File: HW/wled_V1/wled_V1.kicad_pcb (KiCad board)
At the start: 2 copper layers, 44.6 x 77.3 mm, 25 parts, among them J1 0031.8201, U3 TXS0102DCT

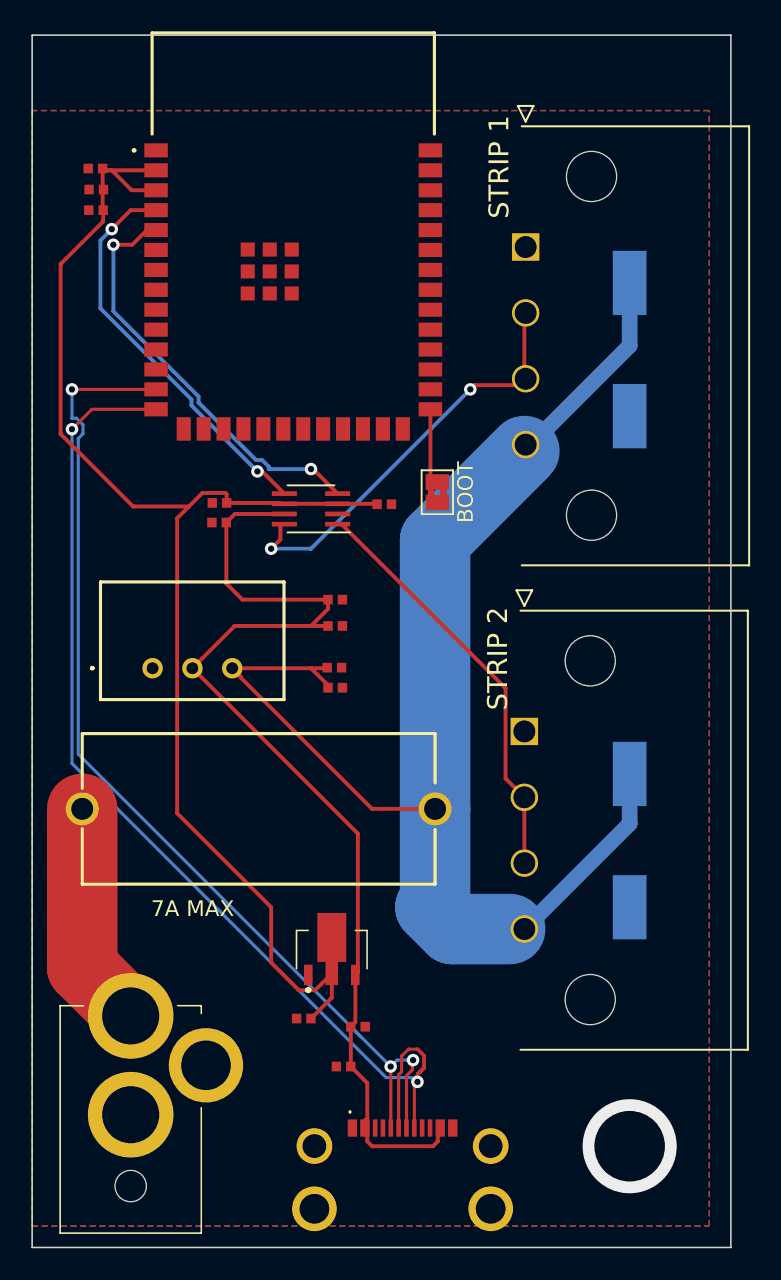
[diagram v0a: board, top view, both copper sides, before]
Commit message: new parts and routing
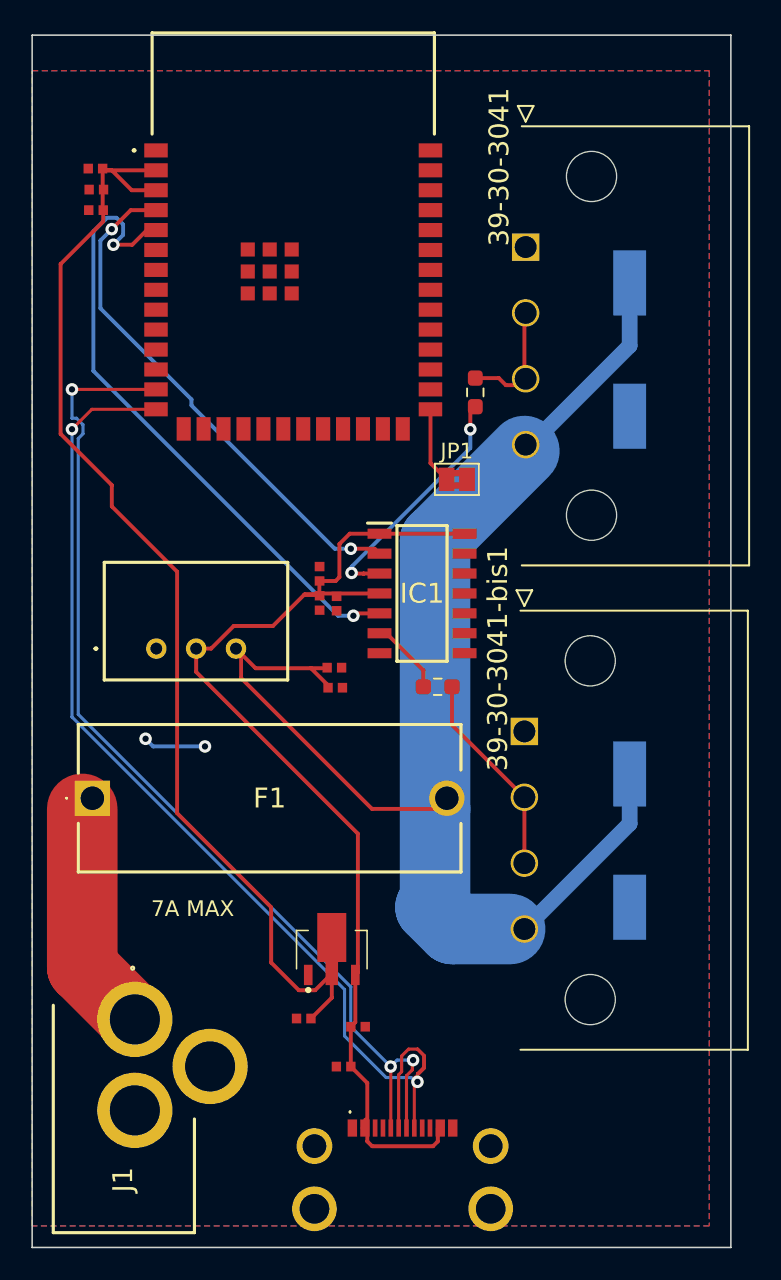
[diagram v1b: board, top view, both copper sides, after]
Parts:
- removed C2, C6: 100nF, SamacSys_Parts:CAPC1005X55N
- removed PJ-057AH1: Jack-DC, SamacSys_Parts:PJ057AH
- removed U3: TXS0102DCT, Package_SO:SSOP-8_2.95x2.8mm_P0.65mm
- added F1: BK1_HTC-100M, SamacSys_Parts:BK1HTC100M, F.Cu at (108.0, 117.5)
- added IC1: SN74AHCT125DR, SamacSys_Parts:SOIC127P600X175-14N, F.Cu at (129.0, 104.5)
- added R1: 0, Resistor_SMD:R_0603_1608Metric_Pad0.98x0.95mm_HandSolder, F.Cu at (132.4, 91.6)
- added R2: 0, Resistor_SMD:R_0603_1608Metric_Pad0.98x0.95mm_HandSolder, F.Cu at (130.0, 110.4)
- 39-30-3041: renamed from STRIP 1
- 39-30-3041-bis1: renamed from STRIP 2
- C5, C8: footprint SamacSys_Parts:CAPAE1030X1030N -> SamacSys_Parts:CAPAE1030X1050N
- J1: value 0031.8201 -> 694106301002; footprint SamacSys_Parts:0031.8201 -> SamacSys_Parts:694106301002_1
- moved J1 27.3 mm to (114.5, 145.2), turned to 90 degrees
- moved C4 9.10 mm to (123.6, 105.1), turned to -90 degrees
- moved C1 1.93 mm to (122.5, 103.2), turned to 90 degrees
- moved C12 1.77 mm to (122.5, 105.1), turned to -90 degrees
- moved JP1 1.49 mm to (131.2, 97.2), turned to 0 degrees
- moved TSR-1-2450 1.27 mm to (112.1, 108.0)
- renumbered BOOT to JP1
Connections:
- J1 pad 2: +12V -> GND
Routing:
- net Net-(39-30-3041-Pin_2): track 26.5 -> 7.52 mm, vias 2 -> 0
- net +3.3V: track 88.9 -> 72.8 mm
- net D3_5V: track 0.00 -> 15.3 mm, vias 0 -> 2
- net D4: track 26.8 -> 40.2 mm
- net Net-(39-30-3041-bis1-Pin_2): track 26.4 -> 13.2 mm
- net D3: track 25.5 -> 33.2 mm
- net D4_5V: track 0.00 -> 4.39 mm
- net GND: track 0.44 -> 3.99 mm, vias 0 -> 2
- net Net-(J1-POWER): track 16.1 -> 14.5 mm
- net +5V: track 68.0 -> 69.0 mm
- net D-: track 68.4 -> 67.4 mm
- net (no net): vias 1 -> 0

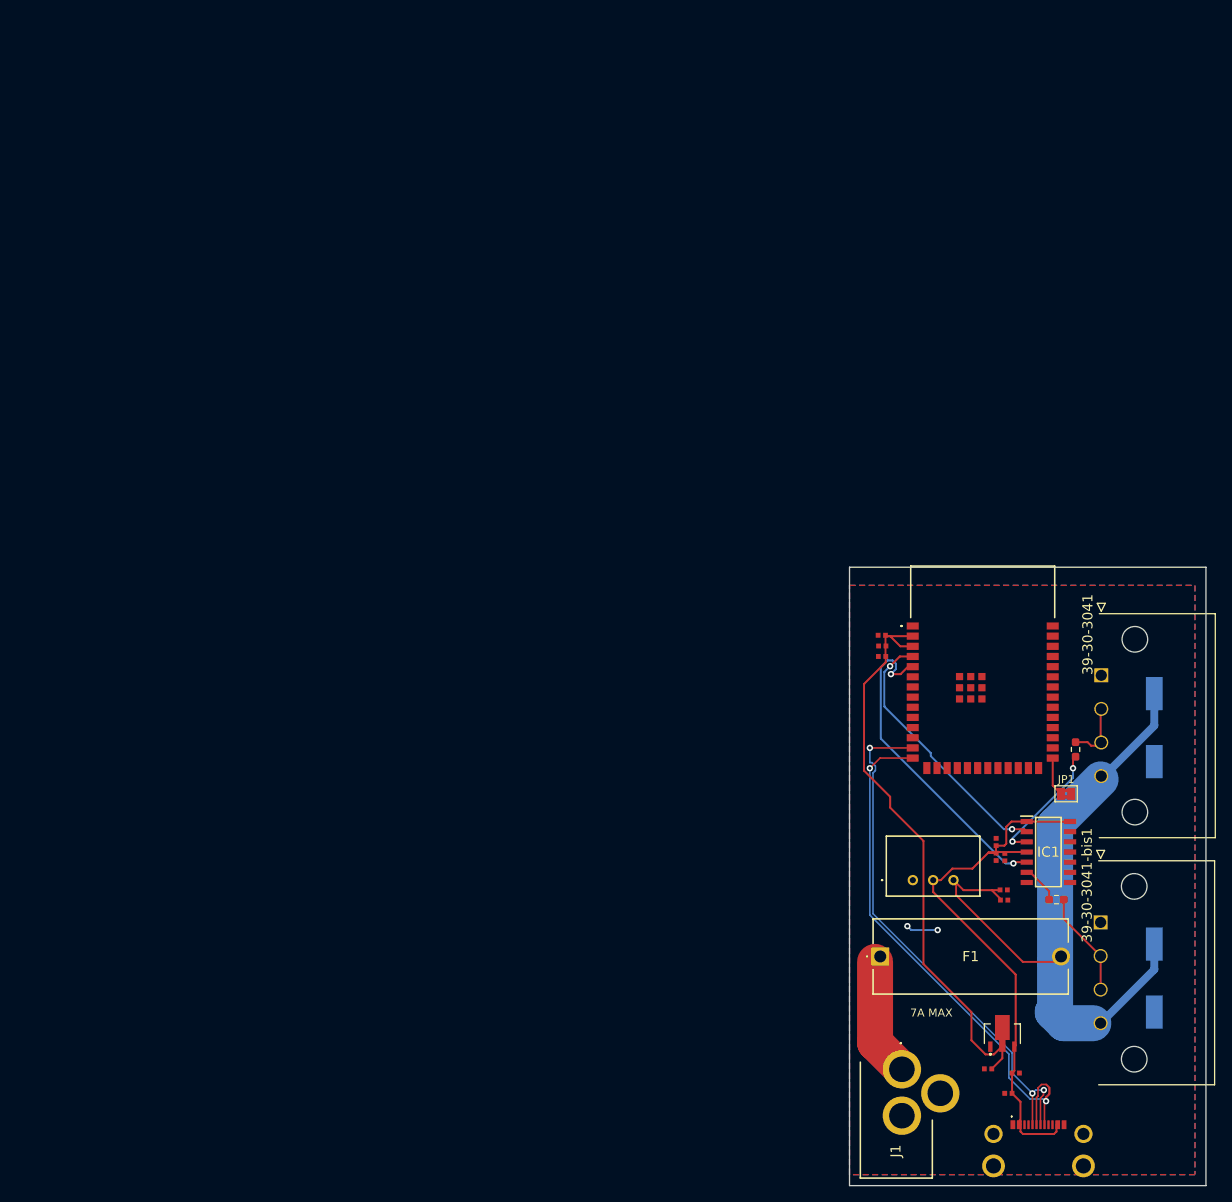
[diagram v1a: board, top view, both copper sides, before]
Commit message: mounting points added
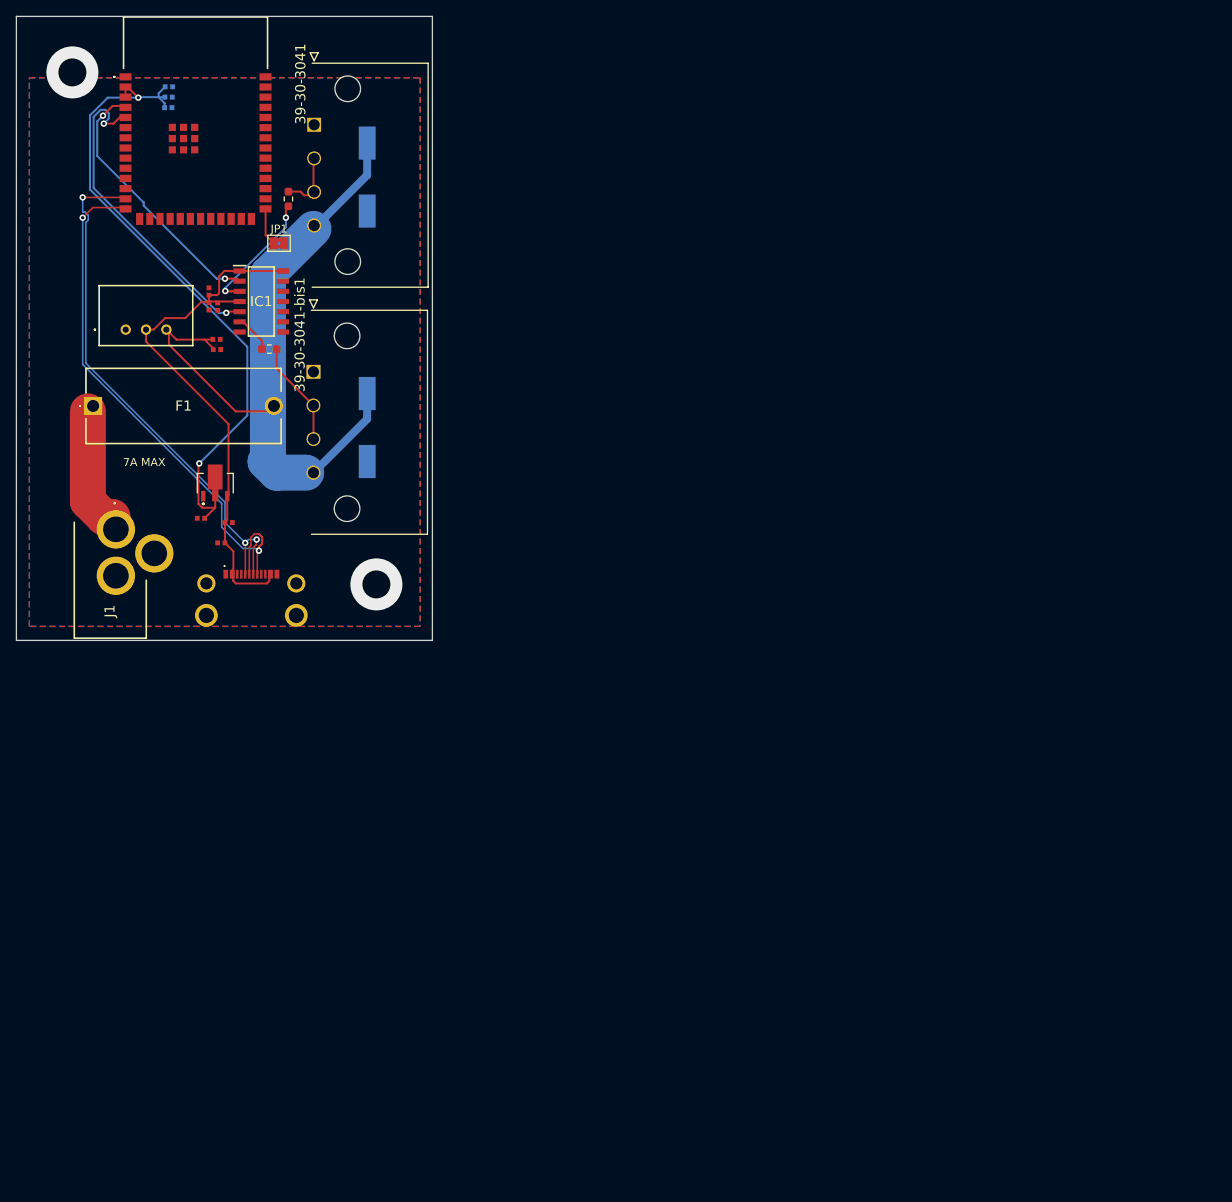
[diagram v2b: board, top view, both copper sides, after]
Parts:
- C0402C103K1RACAUTO1, C10, C14: moved to B.Cu
- moved C11 120.1 mm to (26.5, 63.3)
- moved C4 120.1 mm to (25.2, 36.3)
- moved C8 120.1 mm to (43.8, 20.1)
- moved C9 120.1 mm to (25.6, 65.8)
- moved 39-30-3041 120.1 mm to (37.2, 13.5)
- moved 39-30-3041-bis1 120.1 mm to (37.1, 44.4)
- moved C15 120.1 mm to (23.1, 62.7)
- moved IC1 120.1 mm to (30.6, 35.6)
- moved R2 120.1 mm to (31.6, 41.6)
- moved AZ1117CR-3.3TRG1 120.1 mm to (24.9, 57.1)
- moved C1 120.1 mm to (24.1, 34.4)
- moved C12 120.1 mm to (24.1, 36.2)
- moved C13 120.1 mm to (25.1, 41.6)
- moved C3 120.1 mm to (25.0, 40.4)
- moved C5 120.1 mm to (43.8, 51.4)
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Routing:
- net +3.3V: track 72.8 -> 82.0 mm, vias 0 -> 2
- net GND: track 3.99 -> 1.40 mm
- net Net-(J1-POWER): track 14.5 -> 15.1 mm
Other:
- board size 44.6 x 77.3 mm -> 52 x 78 mm

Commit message: route
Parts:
- added D1: 1N4148W_R1_00001, SamacSys_Parts:SOD3816X135N, F.Cu at (21.9, 64.4)
- added K1: AHQSH112LM1F00G, SamacSys_Parts:AHQSH112LM1F00G, F.Cu at (15.8, 60.1)
- added Q1: MMBT3904-7-F, SamacSys_Parts:SOT96P240X110-3N, F.Cu at (27.1, 64.5)
- added RN73H1JTTD1002F1: 10k, Resistor_SMD:R_0603_1608Metric_Pad0.98x0.95mm_HandSolder, F.Cu at (5.99, 17.8)
- added RN73H1JTTD1002F50: 10k, Resistor_SMD:R_0603_1608Metric_Pad0.98x0.95mm_HandSolder, F.Cu at (28.1, 61.3)
- added S1: TS14-1212-140-BK-160-SCR-D, SamacSys_Parts:TS0266160BK260LCRD, F.Cu at (9.83, 30.5)
- moved F1 12.4 mm to (7.62, 61.0), turned to 90 degrees
- moved C15 12.0 mm to (31.5, 54.3), turned to -90 degrees
- moved C13 11.2 mm to (25.1, 30.5)
- moved C3 11.1 mm to (25.1, 29.2)
- moved AZ1117CR-3.3TRG1 11.1 mm to (31.5, 48.3)
- moved C11 11.1 mm to (33.0, 54.3), turned to -90 degrees
- moved TSR-1-2450 6.85 mm to (20.3, 37.3), turned to 90 degrees
- moved C9 6.10 mm to (31.3, 68.0)
- moved 216990-0002 1.26 mm to (29.4, 73.8)
- moved J1 1.02 mm to (16.2, 78.7)
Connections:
- 39-30-3041 pad 4: +12V -> 12v_commuted
- 39-30-3041-bis1 pad 4: +12V -> 12v_commuted
- C5 pad 1: +12V -> 12v_commuted
- C8 pad 2: +12V -> 12v_commuted
- ESP32-S3-WROOM-1-N8 pad 31: unconnected-(ESP32-S3-WROOM-1-N8-GPIO38/FSPIWP/SUBSPIWP-Pad31) -> D6
- ESP32-S3-WROOM-1-N8 pad 7: D6 -> GPIO7
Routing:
- net D6: track 0.00 -> 89.9 mm, vias 0 -> 2
- net 12v_commuted: track 0.00 -> 80.2 mm
- net GPIO7: track 0.00 -> 23.2 mm
- net GND: track 1.40 -> 22.9 mm
- net +12V: track 88.2 -> 69.8 mm
- net +3.3V: track 82.0 -> 95.3 mm
- net +5V: track 69.0 -> 81.9 mm
- net Net-(D1-A): track 0.00 -> 9.00 mm
- net Net-(J1-POWER): track 15.1 -> 6.55 mm
- net D-: track 67.4 -> 71.7 mm, vias 3 -> 2
- net Net-(Q1-B): track 0.00 -> 2.71 mm
- net D+: track 71.4 -> 72.4 mm
